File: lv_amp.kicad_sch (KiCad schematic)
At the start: 85 parts, among them J1 Jack-DC, J2 AudioJack2, J3 AudioJack2, Q1 Q_NMOS_DGS, U1 MAX1771xSA, U2 TL072, U3 ECC83, U4 ECC83, U5 ECC83

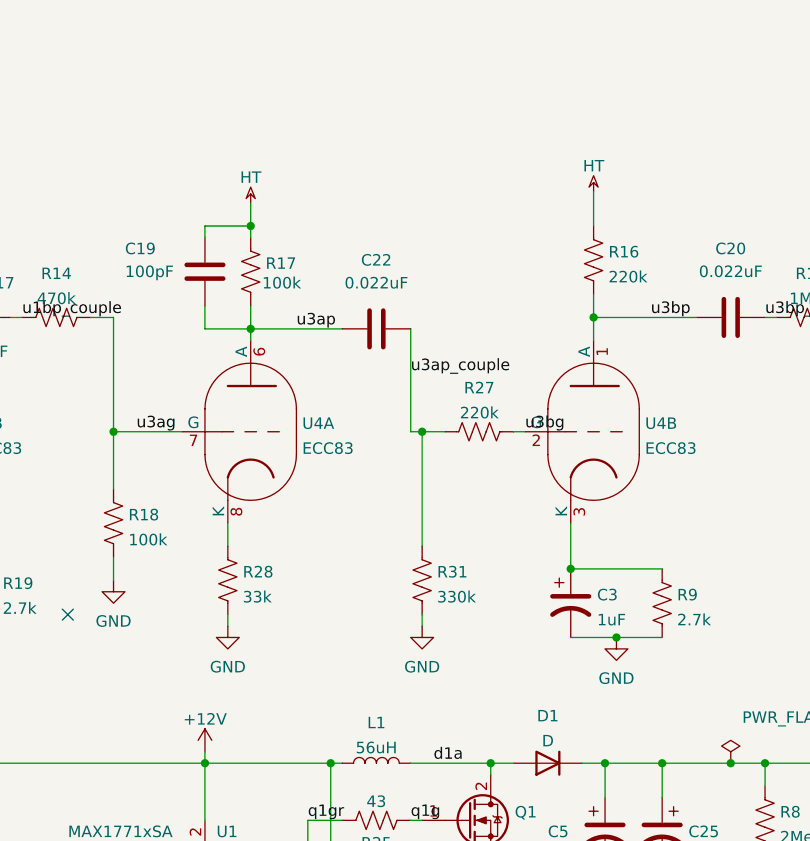
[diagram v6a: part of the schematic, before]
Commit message: alpha0 errata: add 0ohm resistor for easier modding of stage 4
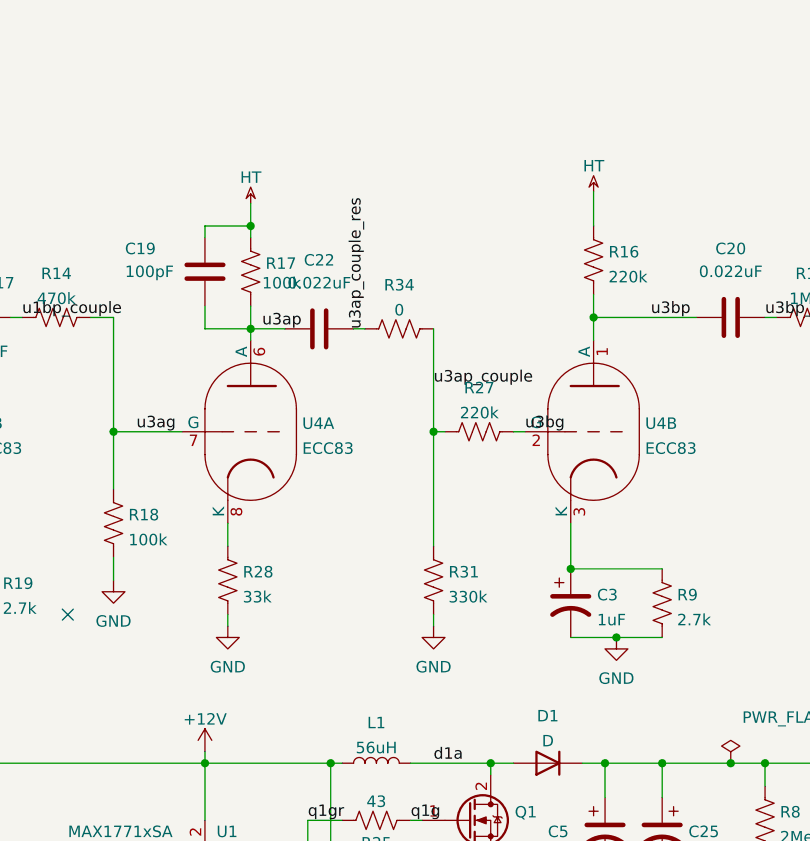
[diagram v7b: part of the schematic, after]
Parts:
- added R34: 0, Resistor_SMD:R_1210_3225Metric, symbol Device:R_US
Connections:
- net u3ap_couple: now also R34.1; no longer C22.2
- new net u3ap_couple_res: C22.2, R34.2
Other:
- moved on the sheet: C22, R31
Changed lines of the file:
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@@
   (junction (at 163.83 153.67) (diameter 0) (color 0 0 0 0)
   )
-  (junction (at 173.99 82.55) (diameter 0) (color 0 0 0 0)
-  )
   (junction (at 85.09 157.48) (diameter 0) (color 0 0 0 0)
   )
@@
   (junction (at 118.11 69.85) (diameter 0) (color 0 0 0 0)
   )
+  (junction (at 175.26 82.55) (diameter 0) (color 0 0 0 0)
+  )
   (junction (at 26.67 81.28) (diameter 0) (color 0 0 0 0)
   )
@@
     (stroke (width 0) (type default) (color 0 0 0 0))
   )
+  (wire (pts (xy 166.37 71.12) (xy 167.64 71.12))
+    (stroke (width 0) (type default) (color 0 0 0 0))
+  )
   (wire (pts (xy 36.83 143.51) (xy 38.1 143.51))
     (stroke (width 0) (type default) (color 0 0 0 0))
@@
     (stroke (width 0) (type default) (color 0 0 0 0))
   )
+  (wire (pts (xy 175.26 71.12) (xy 175.26 82.55))
+    (stroke (width 0) (type default) (color 0 0 0 0))
+  )
   (wire (pts (xy 115.57 92.71) (xy 115.57 96.52))
     (stroke (width 0) (type default) (color 0 0 0 0))
@@
     (stroke (width 0) (type default) (color 0 0 0 0))
   )
-  (wire (pts (xy 172.72 82.55) (xy 173.99 82.55))
-    (stroke (width 0) (type default) (color 0 0 0 0))
-  )
   (wire (pts (xy 59.69 71.12) (xy 59.69 72.39))
     (stroke (width 0) (type default) (color 0 0 0 0))
@@
     (stroke (width 0) (type default) (color 0 0 0 0))
   )
-  (wire (pts (xy 173.99 82.55) (xy 173.99 95.25))
+  (wire (pts (xy 175.26 82.55) (xy 175.26 95.25))
     (stroke (width 0) (type default) (color 0 0 0 0))
   )
@@
     (stroke (width 0) (type default) (color 0 0 0 0))
   )
-  (wire (pts (xy 154.94 71.12) (xy 165.1 71.12))
+  (wire (pts (xy 154.94 71.12) (xy 158.75 71.12))
     (stroke (width 0) (type default) (color 0 0 0 0))
   )
@@
     (stroke (width 0) (type default) (color 0 0 0 0))
   )
-  (wire (pts (xy 172.72 71.12) (xy 172.72 82.55))
-    (stroke (width 0) (type default) (color 0 0 0 0))
-  )
   (wire (pts (xy 50.8 165.1) (xy 50.8 177.8))
     (stroke (width 0) (type default) (color 0 0 0 0))
@@
     (stroke (width 0) (type default) (color 0 0 0 0))
   )
-  (wire (pts (xy 173.99 82.55) (xy 176.53 82.55))
+  (wire (pts (xy 175.26 82.55) (xy 176.53 82.55))
     (stroke (width 0) (type default) (color 0 0 0 0))
   )
@@
     (stroke (width 0) (type default) (color 0 0 0 0))
   )
-  (wire (pts (xy 173.99 102.87) (xy 173.99 104.14))
+  (wire (pts (xy 175.26 102.87) (xy 175.26 104.14))
     (stroke (width 0) (type default) (color 0 0 0 0))
   )
@@
     (effects (font (size 1.27 1.27)) (justify left bottom))
   )
-  (label "u3ap_couple" (at 172.72 76.2 0)
+  (label "u3ap_couple" (at 175.26 77.47 0)
     (effects (font (size 1.27 1.27)) (justify left bottom))
   )
@@
     (effects (font (size 1.27 1.27)) (justify left bottom))
   )
-  (label "u3ap" (at 160.02 71.12 0)
+  (label "u3ap" (at 156.21 71.12 0)
     (effects (font (size 1.27 1.27)) (justify left bottom))
   )
@@
     (effects (font (size 1.27 1.27)) (justify left bottom))
   )
+  (label "u3ap_couple_res" (at 167.64 71.12 90)
+    (effects (font (size 1.27 1.27)) (justify left bottom))
+  )
   (symbol (lib_id "Device:C") (at 124.46 69.85 90) (unit 1)
     (in_bom yes) (on_board yes)
@@
     (pin "3")
   )
-  (symbol (lib_id "power:GND") (at 173.99 104.14 0) (unit 1)
+  (symbol (lib_id "power:GND") (at 175.26 104.14 0) (unit 1)
     (in_bom yes) (on_board yes) (fields_autoplaced)
-    (property "Reference" "#PWR032" (id 0) (at 173.99 110.49 0)
+    (property "Reference" "#PWR032" (id 0) (at 175.26 110.49 0)
       (effects (font (size 1.27 1.27)) hide)
     )
-    (property "Value" "GND" (id 1) (at 173.99 108.7025 0))
-    (property "Footprint" "" (id 2) (at 173.99 104.14 0)
+    (property "Value" "GND" (id 1) (at 175.26 108.7025 0))
+    (property "Footprint" "" (id 2) (at 175.26 104.14 0)
       (effects (font (size 1.27 1.27)) hide)
     )
-    (property "Datasheet" "" (id 3) (at 173.99 104.14 0)
+    (property "Datasheet" "" (id 3) (at 175.26 104.14 0)
       (effects (font (size 1.27 1.27)) hide)
     )
@@
     (pin "1")
   )
-  (symbol (lib_id "Device:C") (at 168.91 71.12 90) (unit 1)
+  (symbol (lib_id "Device:C") (at 162.56 71.12 90) (unit 1)
     (in_bom yes) (on_board yes) (fields_autoplaced)
-    (property "Reference" "C22" (id 0) (at 168.91 63.5 90))
-    (property "Value" "0.022uF" (id 1) (at 168.91 66.04 90))
-    (property "Footprint" "Capacitor_THT:C_Rect_L13.0mm_W4.0mm_P10.00mm_FKS3_FKP3_MKS4" (id 2) (at 172.72 70.1548 0)
+    (property "Reference" "C22" (id 0) (at 162.56 63.5 90))
+    (property "Value" "0.022uF" (id 1) (at 162.56 66.04 90))
+    (property "Footprint" "Capacitor_THT:C_Rect_L13.0mm_W4.0mm_P10.00mm_FKS3_FKP3_MKS4" (id 2) (at 166.37 70.1548 0)
       (effects (font (size 1.27 1.27)) hide)
     )
-    (property "Datasheet" "~" (id 3) (at 168.91 71.12 0)
+    (property "Datasheet" "~" (id 3) (at 162.56 71.12 0)
       (effects (font (size 1.27 1.27)) hide)
     )
@@
     (pin "2")
   )
-  (symbol (lib_id "Device:R_US") (at 173.99 99.06 180) (unit 1)
+  (symbol (lib_id "Device:R_US") (at 175.26 99.06 180) (unit 1)
     (in_bom yes) (on_board yes) (fields_autoplaced)
-    (property "Reference" "R31" (id 0) (at 175.641 98.1515 0)
+    (property "Reference" "R31" (id 0) (at 176.911 98.1515 0)
       (effects (font (size 1.27 1.27)) (justify right))
     )
-    (property "Value" "330k" (id 1) (at 175.641 100.9266 0)
+    (property "Value" "330k" (id 1) (at 176.911 100.9266 0)
       (effects (font (size 1.27 1.27)) (justify right))
     )
-    (property "Footprint" "Resistor_SMD:R_1210_3225Metric" (id 2) (at 172.974 98.806 90)
+    (property "Footprint" "Resistor_SMD:R_1210_3225Metric" (id 2) (at 174.244 98.806 90)
       (effects (font (size 1.27 1.27)) hide)
     )
-    (property "Datasheet" "~" (id 3) (at 173.99 99.06 0)
+    (property "Datasheet" "~" (id 3) (at 175.26 99.06 0)
       (effects (font (size 1.27 1.27)) hide)
     )
@@
     (pin "1")
   )
+  (symbol (lib_id "Device:R_US") (at 171.45 71.12 270) (unit 1)
+    (in_bom yes) (on_board yes) (fields_autoplaced)
+    (property "Reference" "R34" (id 0) (at 171.45 66.2645 90))
+    (property "Value" "0" (id 1) (at 171.45 69.0396 90))
+    (property "Footprint" "Resistor_SMD:R_1210_3225Metric" (id 2) (at 171.196 72.136 90)
+      (effects (font (size 1.27 1.27)) hide)
+    )
+    (property "Datasheet" "~" (id 3) (at 171.45 71.12 0)
+      (effects (font (size 1.27 1.27)) hide)
+    )
+    (pin "1")
+    (pin "2")
+  )
   (symbol (lib_id "Device:R_US") (at 217.17 69.85 90) (unit 1)
     (in_bom yes) (on_board yes) (fields_autoplaced)
@@
       (reference "R33") (unit 1) (value "470k") (footprint "Resistor_SMD:R_1206_3216Metric")
     )
+    (path "/f1a2c47e-279d-4f22-b058-29a2ce1d9b05"
+      (reference "R34") (unit 1) (value "0") (footprint "Resistor_SMD:R_1210_3225Metric")
+    )
     (path "/4537a5c1-2eca-45e3-824f-5f450b04aaa3"

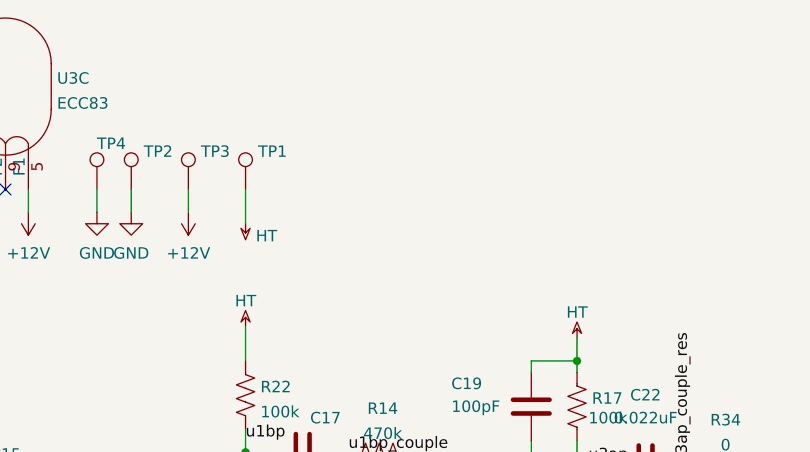
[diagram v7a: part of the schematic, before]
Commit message: alpha0 errata: add slot for load resistor for testing
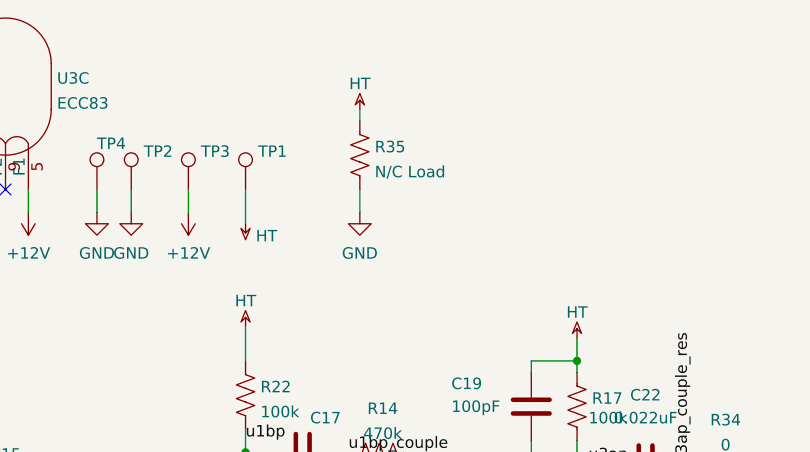
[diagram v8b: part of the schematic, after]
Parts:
- added R35: N/C Load, Resistor_THT:R_Axial_DIN0309_L9.0mm_D3.2mm_P15.24mm_Horizontal, symbol Device:R_US
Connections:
- net GND: now also R35.2
- net HT: now also R35.1
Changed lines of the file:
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@@
     (stroke (width 0) (type default) (color 0 0 0 0))
   )
+  (wire (pts (xy 130.81 31.75) (xy 130.81 33.02))
+    (stroke (width 0) (type default) (color 0 0 0 0))
+  )
   (wire (pts (xy 147.32 179.07) (xy 147.32 172.72))
     (stroke (width 0) (type default) (color 0 0 0 0))
@@
     (stroke (width 0) (type default) (color 0 0 0 0))
   )
+  (wire (pts (xy 130.81 40.64) (xy 130.81 43.18))
+    (stroke (width 0) (type default) (color 0 0 0 0))
+  )
   (wire (pts (xy 176.53 140.97) (xy 176.53 143.51))
     (stroke (width 0) (type default) (color 0 0 0 0))
@@
     (pin "2")
   )
+  (symbol (lib_id "power:HT") (at 130.81 31.75 0) (unit 1)
+    (in_bom yes) (on_board yes) (fields_autoplaced)
+    (property "Reference" "#PWR0103" (id 0) (at 130.81 28.702 0)
+      (effects (font (size 1.27 1.27)) hide)
+    )
+    (property "Value" "HT" (id 1) (at 130.81 28.9075 0))
+    (property "Footprint" "" (id 2) (at 130.81 31.75 0)
+      (effects (font (size 1.27 1.27)) hide)
+    )
+    (property "Datasheet" "" (id 3) (at 130.81 31.75 0)
+      (effects (font (size 1.27 1.27)) hide)
+    )
+    (pin "1")
+  )
   (symbol (lib_id "Device:R_US") (at 168.91 125.73 90) (unit 1)
     (in_bom yes) (on_board yes)
@@
     (pin "1")
   )
+  (symbol (lib_id "power:GND") (at 130.81 43.18 0) (unit 1)
+    (in_bom yes) (on_board yes) (fields_autoplaced)
+    (property "Reference" "#PWR0104" (id 0) (at 130.81 49.53 0)
+      (effects (font (size 1.27 1.27)) hide)
+    )
+    (property "Value" "GND" (id 1) (at 130.81 47.7425 0))
+    (property "Footprint" "" (id 2) (at 130.81 43.18 0)
+      (effects (font (size 1.27 1.27)) hide)
+    )
+    (property "Datasheet" "" (id 3) (at 130.81 43.18 0)
+      (effects (font (size 1.27 1.27)) hide)
+    )
+    (pin "1")
+  )
   (symbol (lib_id "Device:R_US") (at 49.53 137.16 0) (unit 1)
     (in_bom yes) (on_board yes)
@@
     (pin "2")
   )
+  (symbol (lib_id "Device:R_US") (at 130.81 36.83 0) (unit 1)
+    (in_bom yes) (on_board yes) (fields_autoplaced)
+    (property "Reference" "R35" (id 0) (at 132.461 35.9215 0)
+      (effects (font (size 1.27 1.27)) (justify left))
+    )
+    (property "Value" "N/C Load" (id 1) (at 132.461 38.6966 0)
+      (effects (font (size 1.27 1.27)) (justify left))
+    )
+    (property "Footprint" "Resistor_THT:R_Axial_DIN0309_L9.0mm_D3.2mm_P15.24mm_Horizontal" (id 2) (at 131.826 37.084 90)
+      (effects (font (size 1.27 1.27)) hide)
+    )
+    (property "Datasheet" "~" (id 3) (at 130.81 36.83 0)
+      (effects (font (size 1.27 1.27)) hide)
+    )
+    (pin "1")
+    (pin "2")
+  )
   (symbol (lib_id "power:GND") (at 120.65 104.14 0) (unit 1)
     (in_bom yes) (on_board yes) (fields_autoplaced)
@@
       (reference "#PWR0102") (unit 1) (value "GND") (footprint "")
     )
+    (path "/9f23c801-6761-4cbf-9cea-8bdaf150c213"
+      (reference "#PWR0103") (unit 1) (value "HT") (footprint "")
+    )
+    (path "/dbb6ea86-684d-422f-90f8-73a7f26e811c"
+      (reference "#PWR0104") (unit 1) (value "GND") (footprint "")
+    )
     (path "/2293eadd-c3e5-4307-aefa-93ff734054c6"
       (reference "C1") (unit 1) (value "10uF") (footprint "Capacitor_SMD:CP_Elec_16x17.5")
@@
       (reference "R34") (unit 1) (value "0") (footprint "Resistor_SMD:R_1210_3225Metric")
     )
+    (path "/eafcf511-2048-4926-8953-a8c65022b125"
+      (reference "R35") (unit 1) (value "N/C Load") (footprint "Resistor_THT:R_Axial_DIN0309_L9.0mm_D3.2mm_P15.24mm_Horizontal")
+    )
     (path "/4537a5c1-2eca-45e3-824f-5f450b04aaa3"
